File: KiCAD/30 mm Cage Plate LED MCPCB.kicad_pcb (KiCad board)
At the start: 2 copper layers, 40 x 40 mm, 13 parts, among them IC1 AL8843QSP-13, J1 Conn_01x04

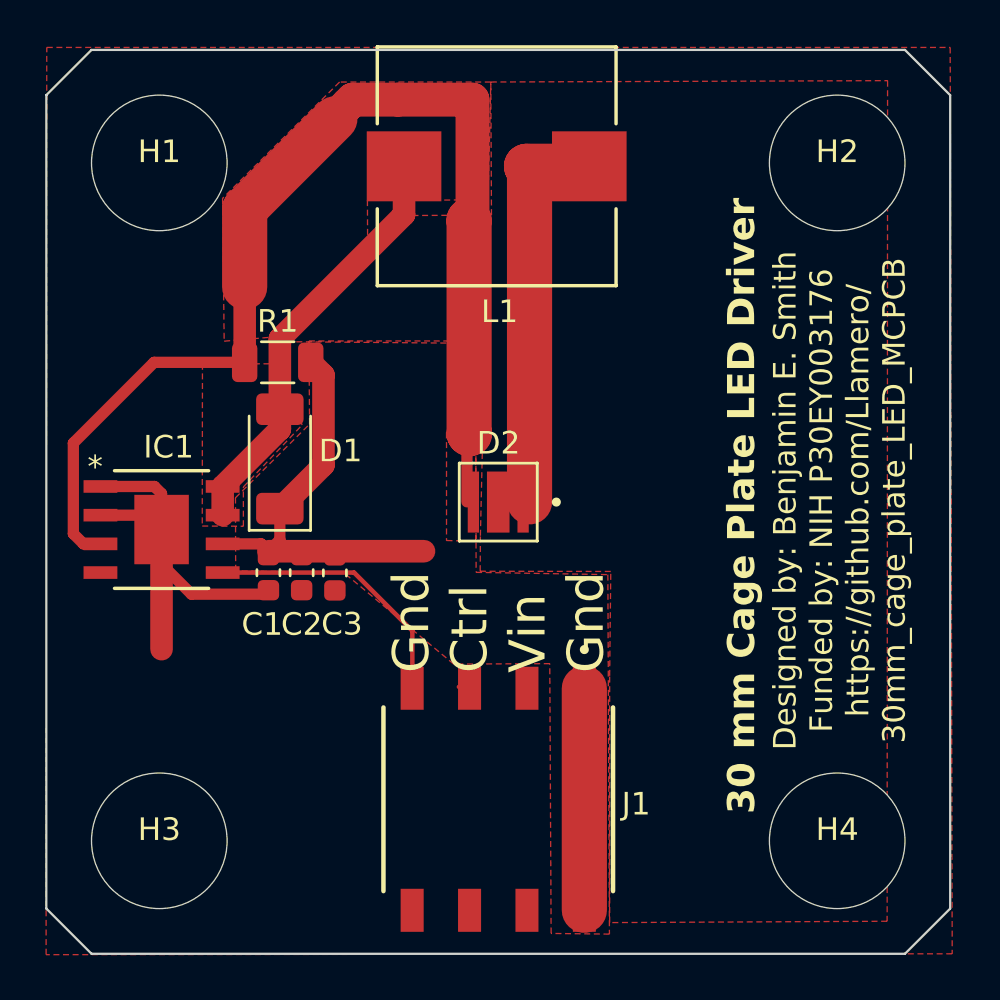
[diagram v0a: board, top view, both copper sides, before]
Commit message: Imrpoved design - more caps and therm
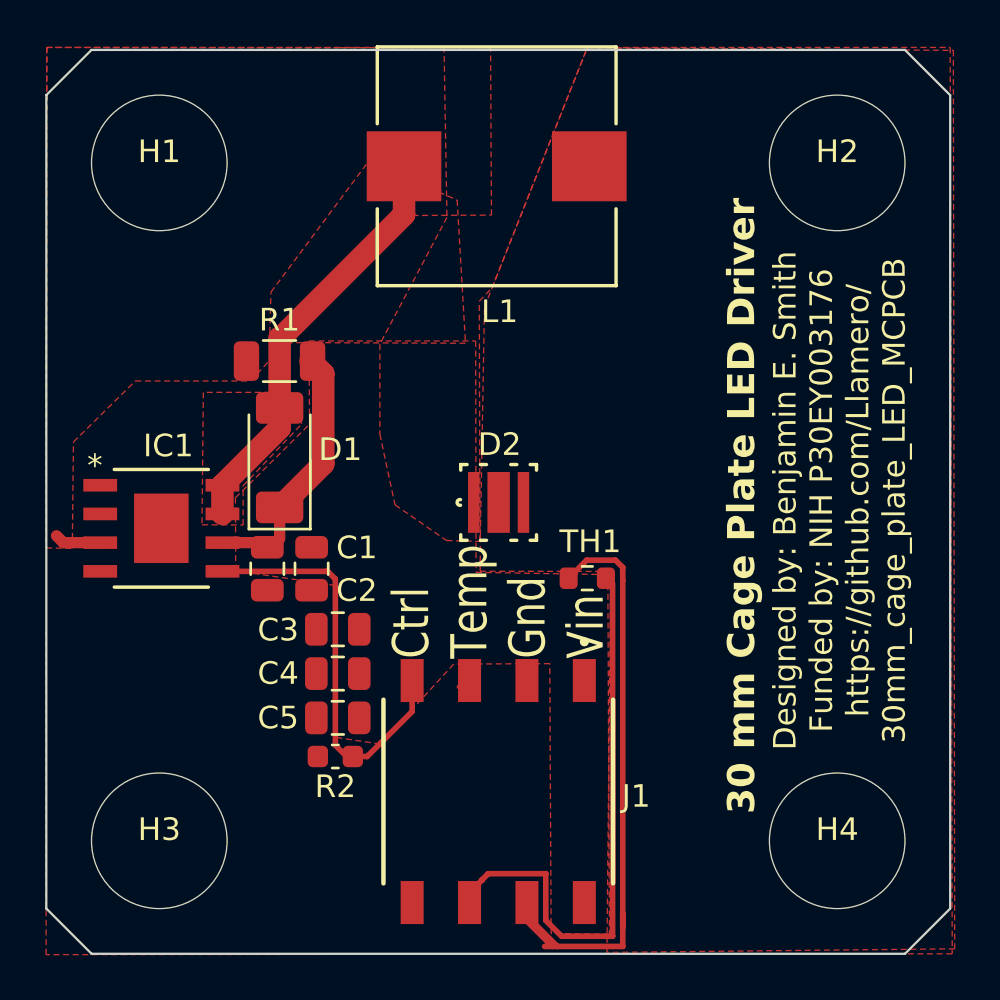
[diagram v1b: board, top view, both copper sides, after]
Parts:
- added C4: 22µF, Capacitor_SMD:C_0805_2012Metric, F.Cu at (112.9, 87.6)
- added C5: 22µF, Capacitor_SMD:C_0805_2012Metric, F.Cu at (112.9, 89.6)
- added R2: 4.7k, Capacitor_SMD:C_0603_1608Metric, F.Cu at (112.8, 91.3)
- added TH1: Thermistor, Resistor_SMD:R_0603_1608Metric, F.Cu at (123.9, 83.4)
- C1, C2, C3: value 10μF -> 22µF; footprint Capacitor_SMD:C_0603_1608Metric -> Capacitor_SMD:C_0805_2012Metric
- D2: footprint Custom:LED_SST-10-IRD-B90H-S810 -> Custom:CSSRML_C69062_AOS
- R1: value 0.068 -> 0.1
- moved C3 2.50 mm to (112.9, 85.6), turned to 0 degrees
- moved C2 0.47 mm to (111.7, 83.0)
- moved J1 0.34 mm to (120.0, 92.8)
- moved C1 0.18 mm to (109.8, 83.0)
- moved R1 0.10 mm to (110.3, 73.8)
- moved D1 0.06 mm to (110.3, 78.0)
- moved IC1 0.06 mm to (105.1, 81.2)
- turned D2 to 0 degrees
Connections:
- IC1 pad 3: Net-(IC1-SET) -> Net-(D2-A)
- J1 pad 3: GND -> Net-(J1-Pin_3)
- L1 pad 1: Net-(D2-PadC) -> Net-(D2-K)
- R1 pad 1: Net-(IC1-SET) -> Net-(D2-A)
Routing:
- net Net-(IC1-SET): track 54.4 -> 0.00 mm
- net Net-(J1-Pin_3): track 0.00 -> 26.1 mm
- net Net-(D2-PadC): track 21.7 -> 0.00 mm
- net /Vin: track 28.5 -> 11.8 mm
- net GND: track 20.5 -> 29.7 mm
- net /PWM: track 12.5 -> 18.3 mm
- net Net-(D2-A): track 0.00 -> 2.06 mm
- added copper zone on F.Cu, net Net-(D2-A)
- added copper zone on F.Cu, net Net-(D2-K)
- removed copper zone on F.Cu, net Net-(D2-PadC)
- removed copper zone on F.Cu, net Net-(IC1-SET)
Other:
- board text added: "Ctrl Temp Gnd Vin"
- board text removed: "Gnd Ctrl Vin Gnd"

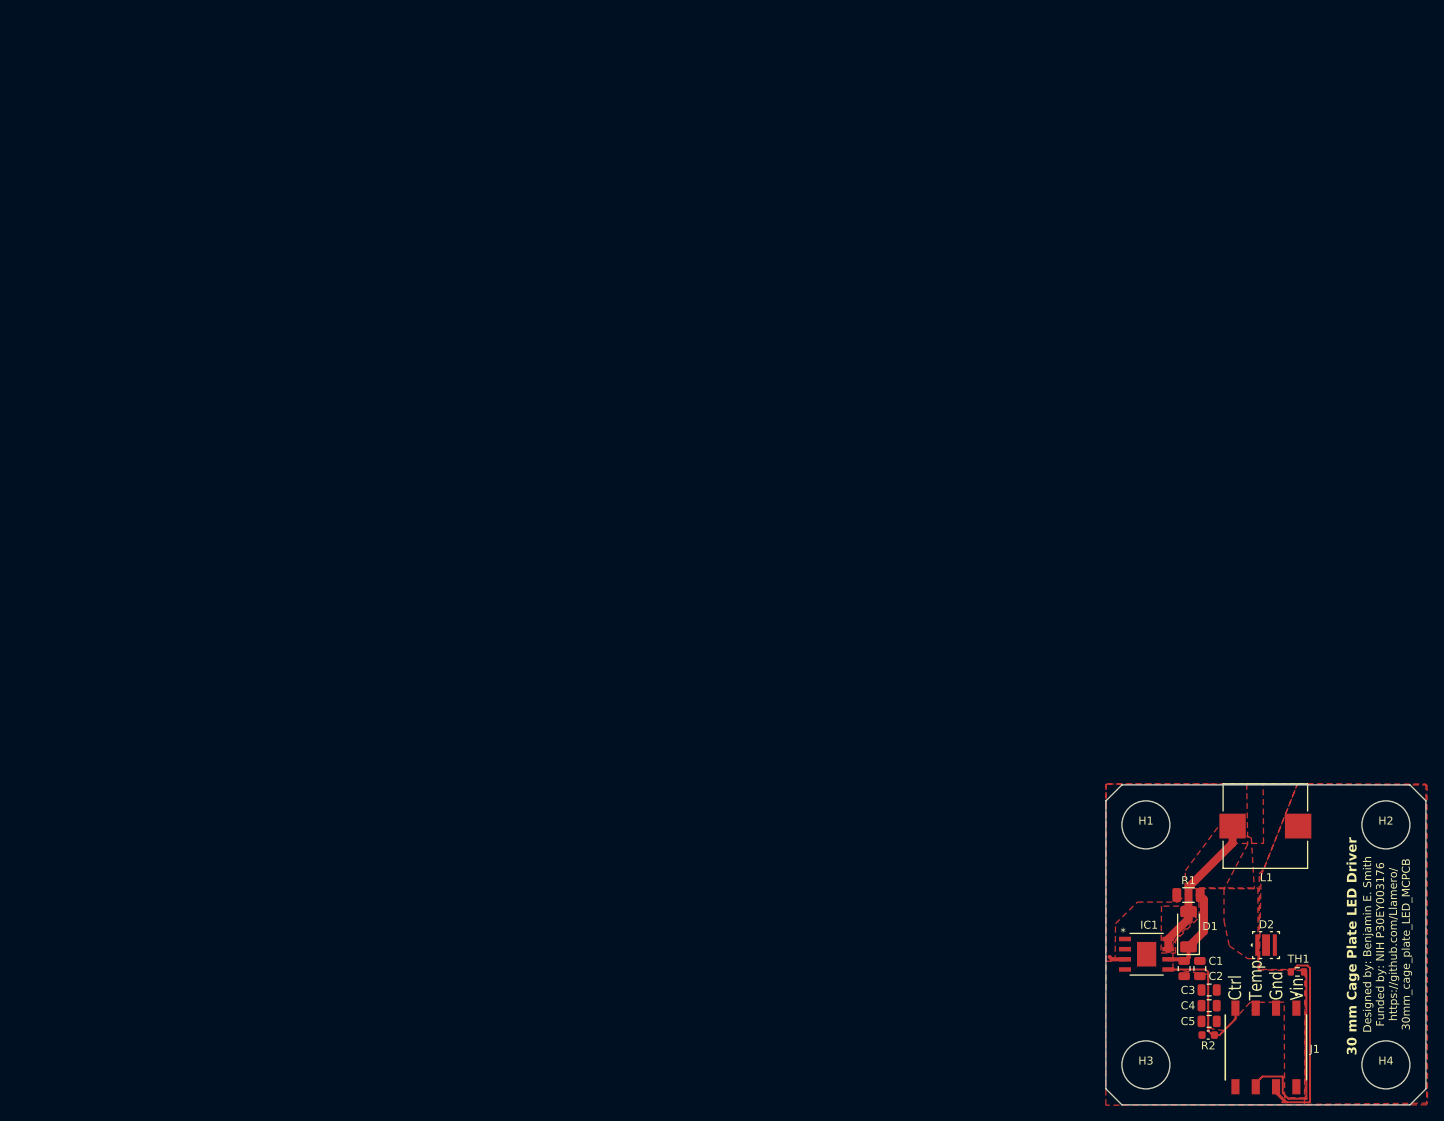
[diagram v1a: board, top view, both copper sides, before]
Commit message: 60 mm plate with flat 8x connector
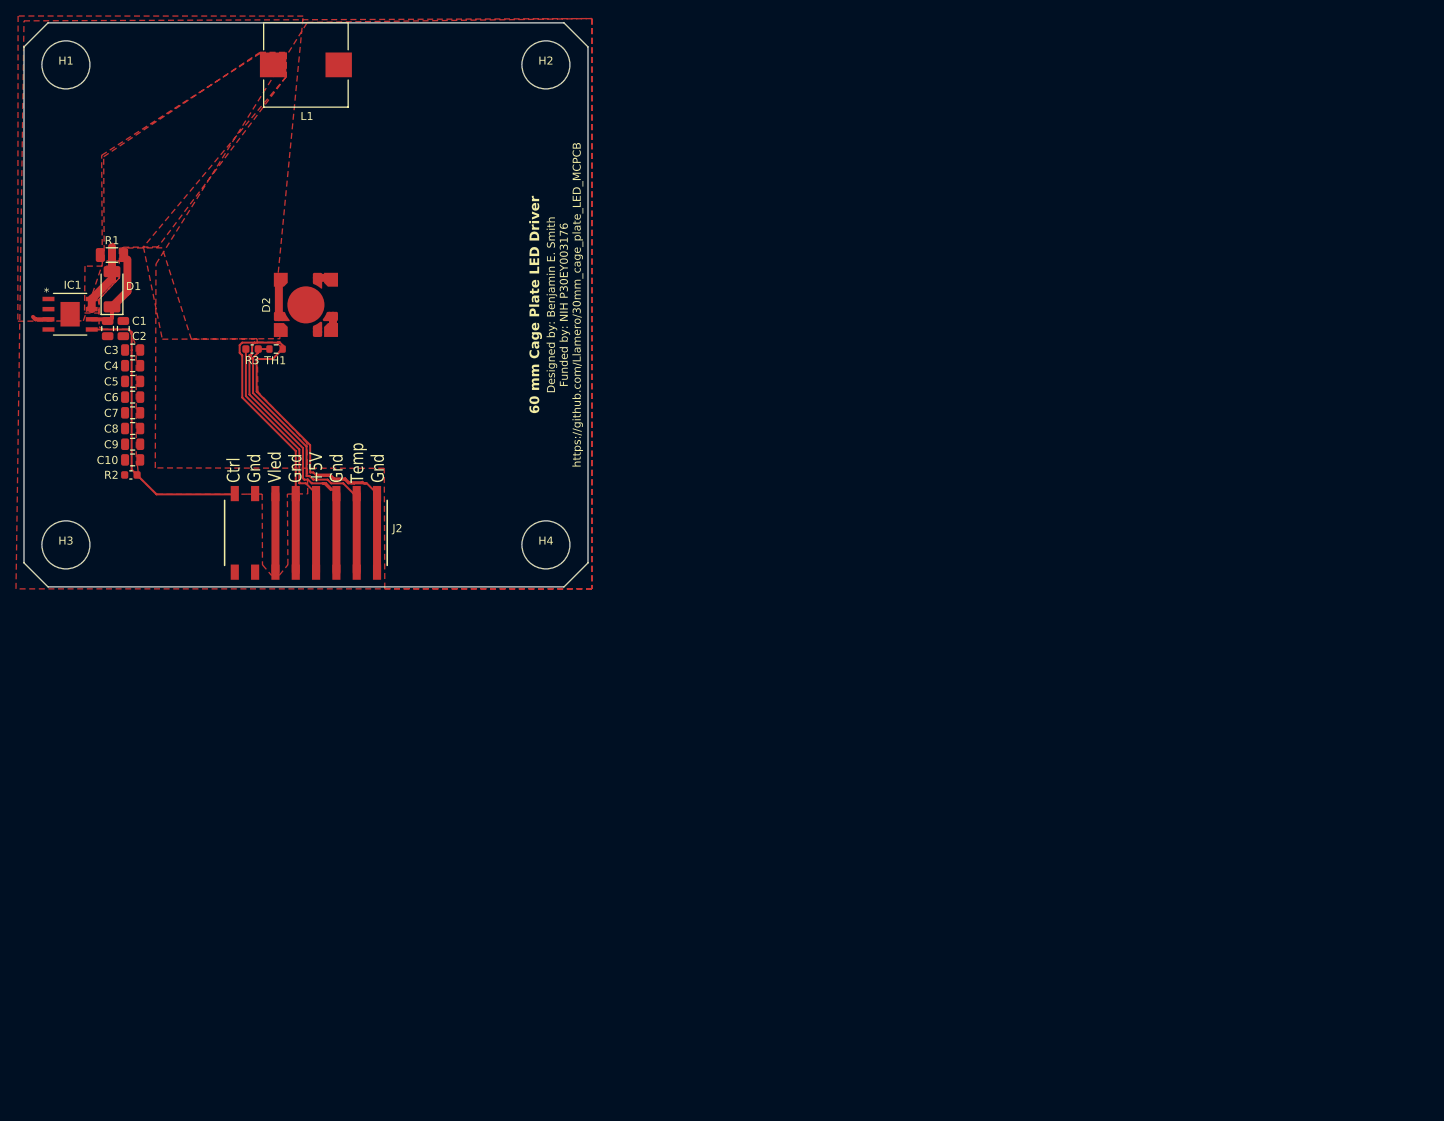
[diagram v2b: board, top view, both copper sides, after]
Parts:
- removed J1: Conn_01x04, Custom:SAMTEC_SSM-104-L-SH
- added C10: 22µF, Capacitor_SMD:C_0805_2012Metric, F.Cu at (-21.7, 19.4)
- added C6: 22µF, Capacitor_SMD:C_0805_2012Metric, F.Cu at (-21.7, 11.5)
- added C7: 22µF, Capacitor_SMD:C_0805_2012Metric, F.Cu at (-21.7, 13.5)
- added C8: 22µF, Capacitor_SMD:C_0805_2012Metric, F.Cu at (-21.7, 15.5)
- added C9: 22µF, Capacitor_SMD:C_0805_2012Metric, F.Cu at (-21.7, 17.4)
- added J2: Conn_01x08_Socket, Custom:SAMTEC_SSM-108-F-SH-TR, F.Cu at (0.00, 28.5)
- added R3: 4.7k, Capacitor_SMD:C_0603_1608Metric, F.Cu at (-6.73, 5.52)
- D2: value SST-10-IRD-B90H-S810 -> LZ4-00; footprint Custom:CSSRML_C69062_AOS -> Custom:LZ4-00
- moved H1 165.1 mm to (-30.0, -30.0)
- moved C1 156.5 mm to (-24.8, 2.96)
- moved C2 156.5 mm to (-22.8, 2.96)
- moved D1 156.5 mm to (-24.2, -1.96)
- moved IC1 156.5 mm to (-29.5, 1.17)
- moved R1 156.5 mm to (-24.2, -6.23)
- moved C3 156.5 mm to (-21.7, 5.64)
- moved C4 156.5 mm to (-21.7, 7.60)
- moved C5 156.5 mm to (-21.7, 9.57)
- moved L1 153.1 mm to (0.00, -30.0)
- moved R2 151.8 mm to (-21.9, 21.3)
- moved H3 149.8 mm to (-30.0, 30.0)
- moved TH1 149.5 mm to (-3.73, 5.52), turned to 0 degrees
- moved D2 144.2 mm to (0.00, 0.00), turned to 90 degrees
- moved H2 141.6 mm to (30.0, -30.0)
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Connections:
- net /PWM renamed /CTRL
- D2 pad 1: Net-(D2-K) -> Net-(IC1-SET)
- D2 pad 2: Net-(D2-A) -> Net-(D2-A-Pad3)
- D2 pad 3: Net-(D2-K) -> Net-(D2-A-Pad3)
- IC1 pad 3: Net-(D2-A) -> Net-(IC1-SET)
- L1 pad 1: Net-(D2-K) -> Net-(D2-PAD)
- R1 pad 1: Net-(D2-A) -> Net-(IC1-SET)
- TH1 pad 1: Net-(J1-Pin_3) -> /Temp
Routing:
- net GND: track 29.7 -> 121.7 mm
- net /Temp: track 0.00 -> 37.3 mm
- net +5V: track 0.00 -> 32.0 mm
- net Net-(J1-Pin_3): track 26.1 -> 0.00 mm
- net /CTRL: track 18.3 -> 36.5 mm
- net Net-(D1-A): track 18.8 -> 8.85 mm
- net /Vin: track 11.8 -> 20.8 mm
- net Net-(D2-A-Pad3): track 0.00 -> 4.69 mm
- net Net-(IC1-SET): track 0.00 -> 2.06 mm
- net Net-(D2-A): track 2.06 -> 0.00 mm
- net Net-(D2-A-Pad7): track 0.00 -> 1.79 mm
- net Net-(D2-A-Pad5): track 0.00 -> 1.79 mm
- added copper zone on F.Cu, net /Temp
- added copper zone on F.Cu, net Net-(D2-PAD)
- added copper zone on F.Cu, net Net-(IC1-SET)
- removed copper zone on F.Cu, net Net-(D2-A)
- removed copper zone on F.Cu, net Net-(D2-K)
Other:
- board size 40 x 40 mm -> 70.5 x 70.5 mm
- board text added: "60 mm Cage Plate LED Driver"
- board text added: "Ctrl Gnd Vled Gnd +5V Gnd Temp Gnd"
- board text added: "Designed by: Benjamin E. Smith Funded by: NIH P30EY003176 https://github.com/Llamero/30mm_cage_plate_LED_MCPCB"
- board text removed: "30 mm Cage Plate LED Driver"
- board text removed: "Ctrl Temp Gnd Vin"
- board text removed: "Designed by: Benjamin E. Smith Funded by: NIH P30EY003176 https://github.com/Llamero/ 30mm_cage_plate_LED_MCPCB"

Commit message: CAD mockup
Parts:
- removed J2: Conn_01x08_Socket, Custom:SAMTEC_SSM-108-F-SH-TR
- removed R3: 4.7k, Capacitor_SMD:C_0603_1608Metric
- added J1: 8P8C_Shielded, Custom:1x RJ45, F.Cu at (0.00, 20.3)
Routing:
- net GND: track 121.7 -> 52.1 mm
- net +5V: track 32.0 -> 0.00 mm
- net /Temp: track 37.3 -> 18.2 mm
- net /CTRL: track 36.5 -> 48.4 mm
- net /Vin: track 20.8 -> 17.3 mm
- removed copper zone on F.Cu, net /Temp
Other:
- board text added: "Ctrl Vled Vled Temp"
- board text removed: "Ctrl Gnd Vled Gnd +5V Gnd Temp Gnd"
